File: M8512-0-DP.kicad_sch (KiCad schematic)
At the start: 1 part, among them J1 KL10_6-bay_backplane_connector

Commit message: Use pin NUMBERS not letters for backplane connector
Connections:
- net AA1: now also J1.1 (AA1); no longer J1.AA1
- net AA2: now also J1.2 (AA2); no longer J1.AA2
- net AB1: now also J1.3 (AB1); no longer J1.AB1
- net AB2: now also J1.4 (AB2); no longer J1.AB2
- net AC1: now also J1.5 (AC1); no longer J1.AC1
- net AC2: now also J1.6 (AC2); no longer J1.AC2
- net AD1: now also J1.7 (AD1); no longer J1.AD1
- net AD2: now also J1.8 (AD2); no longer J1.AD2
- net AE1: now also J1.9 (AE1); no longer J1.AE1
- net AE2: now also J1.10 (AE2); no longer J1.AE2
- net AF1: now also J1.11 (AF1); no longer J1.AF1
- net AF2: now also J1.12 (AF2); no longer J1.AF2
- net AH1: now also J1.13 (AH1); no longer J1.AH1
- net AH2: now also J1.14 (AH2); no longer J1.AH2
- net AJ1: now also J1.15 (AJ1); no longer J1.AJ1
- net AJ2: now also J1.16 (AJ2); no longer J1.AJ2
- net AK1: now also J1.17 (AK1); no longer J1.AK1
- net AK2: now also J1.18 (AK2); no longer J1.AK2
- net AL1: now also J1.19 (AL1); no longer J1.AL1
- net AL2: now also J1.20 (AL2); no longer J1.AL2
- net AM1: now also J1.21 (AM1); no longer J1.AM1
- net AM2: now also J1.22 (AM2); no longer J1.AM2
- net AN1: now also J1.23 (AN1); no longer J1.AN1
- net AN2: now also J1.24 (AN2); no longer J1.AN2
- net AP1: now also J1.25 (AP1); no longer J1.AP1
- net AP2: now also J1.26 (AP2); no longer J1.AP2
- net AR1: now also J1.27 (AR1); no longer J1.AR1
- net AR2: now also J1.28 (AR2); no longer J1.AR2
- net AS1: now also J1.29 (AS1); no longer J1.AS1
- net AS2: now also J1.30 (AS2); no longer J1.AS2
- net AT1: now also J1.31 (AT1); no longer J1.AT1
- net AT2: now also J1.32 (AT2); no longer J1.AT2
- net AU1: now also J1.33 (AU1); no longer J1.AU1
- net AU2: now also J1.34 (AU2); no longer J1.AU2
- net AV1: now also J1.35 (AV1); no longer J1.AV1
- net AV2: now also J1.36 (AV2); no longer J1.AV2
- net BA1: now also J1.37 (BA1); no longer J1.BA1
- net BA2: now also J1.38 (BA2); no longer J1.BA2
- net BB1: now also J1.39 (BB1); no longer J1.BB1
- net BB2: now also J1.40 (BB2); no longer J1.BB2
- net BC1: now also J1.41 (BC1); no longer J1.BC1
- net BC2: now also J1.42 (BC2); no longer J1.BC2
- net BD1: now also J1.43 (BD1); no longer J1.BD1
- net BD2: now also J1.44 (BD2); no longer J1.BD2
- net BE1: now also J1.45 (BE1); no longer J1.BE1
- net BE2: now also J1.46 (BE2); no longer J1.BE2
- net BF1: now also J1.47 (BF1); no longer J1.BF1
- net BF2: now also J1.48 (BF2); no longer J1.BF2
- net BH1: now also J1.49 (BH1); no longer J1.BH1
- net BH2: now also J1.50 (BH2); no longer J1.BH2
- net BJ1: now also J1.51 (BJ1); no longer J1.BJ1
- net BJ2: now also J1.52 (BJ2); no longer J1.BJ2
- net BK1: now also J1.53 (BK1); no longer J1.BK1
- net BK2: now also J1.54 (BK2); no longer J1.BK2
- net BL1: now also J1.55 (BL1); no longer J1.BL1
- net BL2: now also J1.56 (BL2); no longer J1.BL2
- net BM1: now also J1.57 (BM1); no longer J1.BM1
- net BM2: now also J1.58 (BM2); no longer J1.BM2
- net BN1: now also J1.59 (BN1); no longer J1.BN1
- net BN2: now also J1.60 (BN2); no longer J1.BN2
- net BP1: now also J1.61 (BP1); no longer J1.BP1
- net BP2: now also J1.62 (BP2); no longer J1.BP2
- net BR1: now also J1.63 (BR1); no longer J1.BR1
- net BR2: now also J1.64 (BR2); no longer J1.BR2
- net BS1: now also J1.65 (BS1); no longer J1.BS1
- net BS2: now also J1.66 (BS2); no longer J1.BS2
- net BT1: now also J1.67 (BT1); no longer J1.BT1
- net BT2: now also J1.68 (BT2); no longer J1.BT2
- net BU1: now also J1.69 (BU1); no longer J1.BU1
- net BU2: now also J1.70 (BU2); no longer J1.BU2
- net BV1: now also J1.71 (BV1); no longer J1.BV1
- net BV2: now also J1.72 (BV2); no longer J1.BV2
- net CA1: now also J1.73 (CA1); no longer J1.CA1
- net CB1: now also J1.75 (CB1); no longer J1.CB1
- net CB2: now also J1.76 (CB2); no longer J1.CB2
- net CC1: now also J1.77 (CC1); no longer J1.CC1
- net CC2: now also J1.78 (CC2); no longer J1.CC2
- net CD1: now also J1.79 (CD1); no longer J1.CD1
- net CD2: now also J1.80 (CD2); no longer J1.CD2
- net CE1: now also J1.81 (CE1); no longer J1.CE1
- net CE2: now also J1.82 (CE2); no longer J1.CE2
- net CF1: now also J1.83 (CF1); no longer J1.CF1
- net CF2: now also J1.84 (CF2); no longer J1.CF2
- net CH1: now also J1.85 (CH1); no longer J1.CH1
- net CH2: now also J1.86 (CH2); no longer J1.CH2
- net CJ1: now also J1.87 (CJ1); no longer J1.CJ1
- net CJ2: now also J1.88 (CJ2); no longer J1.CJ2
- net CK1: now also J1.89 (CK1); no longer J1.CK1
- net CK2: now also J1.90 (CK2); no longer J1.CK2
- net CL1: now also J1.91 (CL1); no longer J1.CL1
- net CL2: now also J1.92 (CL2); no longer J1.CL2
- net CM1: now also J1.93 (CM1); no longer J1.CM1
- net CM2: now also J1.94 (CM2); no longer J1.CM2
- net CN1: now also J1.95 (CN1); no longer J1.CN1
- net CN2: now also J1.96 (CN2); no longer J1.CN2
- net CP1: now also J1.97 (CP1); no longer J1.CP1
- net CP2: now also J1.98 (CP2); no longer J1.CP2
- net CR1: now also J1.99 (CR1); no longer J1.CR1
- net CR2: now also J1.100 (CR2); no longer J1.CR2
- net CS1: now also J1.101 (CS1); no longer J1.CS1
- net CS2: now also J1.102 (CS2); no longer J1.CS2
- net CT1: now also J1.103 (CT1); no longer J1.CT1
- net CT2: now also J1.104 (CT2); no longer J1.CT2
- net CU1: now also J1.105 (CU1); no longer J1.CU1
- net CU2: now also J1.106 (CU2); no longer J1.CU2
- net CV1: now also J1.107 (CV1); no longer J1.CV1
- net CV2: now also J1.108 (CV2), J1.74 (CA2); no longer J1.CA2, J1.CV2
- net DA1: now also J1.109 (DA1); no longer J1.DA1
- net DA2: now also J1.110 (DA2); no longer J1.DA2
- net DB1: now also J1.111 (DB1); no longer J1.DB1
- net DB2: now also J1.112 (DB2); no longer J1.DB2
- net DC1: now also J1.113 (DC1); no longer J1.DC1
- net DC2: now also J1.114 (DC2); no longer J1.DC2
- net DD1: now also J1.115 (DD1); no longer J1.DD1
- net DD2: now also J1.116 (DD2); no longer J1.DD2
- net DE1: now also J1.117 (DE1); no longer J1.DE1
- net DE2: now also J1.118 (DE2); no longer J1.DE2
- net DF1: now also J1.119 (DF1); no longer J1.DF1
- net DF2: now also J1.120 (DF2); no longer J1.DF2
- net DH1: now also J1.121 (DH1); no longer J1.DH1
- net DH2: now also J1.122 (DH2); no longer J1.DH2
- net DJ1: now also J1.123 (DJ1); no longer J1.DJ1
- net DJ2: now also J1.124 (DJ2); no longer J1.DJ2
- net DK1: now also J1.125 (DK1); no longer J1.DK1
- net DK2: now also J1.126 (DK2); no longer J1.DK2
- net DL1: now also J1.127 (DL1); no longer J1.DL1
- net DL2: now also J1.128 (DL2); no longer J1.DL2
- net DM1: now also J1.129 (DM1); no longer J1.DM1
- net DM2: now also J1.130 (DM2); no longer J1.DM2
- net DN1: now also J1.131 (DN1); no longer J1.DN1
- net DN2: now also J1.132 (DN2); no longer J1.DN2
- net DP1: now also J1.133 (DP1); no longer J1.DP1
- net DP2: now also J1.134 (DP2); no longer J1.DP2
- net DR1: now also J1.135 (DR1); no longer J1.DR1
- net DR2: now also J1.136 (DR2); no longer J1.DR2
- net DS1: now also J1.137 (DS1); no longer J1.DS1
- net DS2: now also J1.138 (DS2); no longer J1.DS2
- net DT1: now also J1.139 (DT1); no longer J1.DT1
- net DT2: now also J1.140 (DT2); no longer J1.DT2
- net DU1: now also J1.141 (DU1); no longer J1.DU1
- net DU2: now also J1.142 (DU2); no longer J1.DU2
- net DV1: now also J1.143 (DV1); no longer J1.DV1
- net DV2: now also J1.144 (DV2); no longer J1.DV2
- net EA1: now also J1.145 (EA1); no longer J1.EA1
- net EA2: now also J1.146 (EA2); no longer J1.EA2
- net EB1: now also J1.147 (EB1); no longer J1.EB1
- net EB2: now also J1.148 (EB2); no longer J1.EB2
- net EC1: now also J1.149 (EC1); no longer J1.EC1
- net EC2: now also J1.150 (EC2); no longer J1.EC2
- net ED1: now also J1.151 (ED1); no longer J1.ED1
- net ED2: now also J1.152 (ED2); no longer J1.ED2
- net EE1: now also J1.153 (EE1); no longer J1.EE1
- net EE2: now also J1.154 (EE2); no longer J1.EE2
- net EF1: now also J1.155 (EF1); no longer J1.EF1
- net EF2: now also J1.156 (EF2); no longer J1.EF2
- net EH1: now also J1.157 (EH1); no longer J1.EH1
- net EH2: now also J1.158 (EH2); no longer J1.EH2
- net EJ1: now also J1.159 (EJ1); no longer J1.EJ1
- net EJ2: now also J1.160 (EJ2); no longer J1.EJ2
- net EK1: now also J1.161 (EK1); no longer J1.EK1
- net EK2: now also J1.162 (EK2); no longer J1.EK2
- net EL1: now also J1.163 (EL1); no longer J1.EL1
- net EL2: now also J1.164 (EL2); no longer J1.EL2
- net EM1: now also J1.165 (EM1); no longer J1.EM1
- net EM2: now also J1.166 (EM2); no longer J1.EM2
- net EN1: now also J1.167 (EN1); no longer J1.EN1
- net EN2: now also J1.168 (EN2); no longer J1.EN2
- net EP1: now also J1.169 (EP1); no longer J1.EP1
- net EP2: now also J1.170 (EP2); no longer J1.EP2
- net ER1: now also J1.171 (ER1); no longer J1.ER1
- net ER2: now also J1.172 (ER2); no longer J1.ER2
- net ES1: now also J1.173 (ES1); no longer J1.ES1
- net ES2: now also J1.174 (ES2); no longer J1.ES2
- net ET1: now also J1.175 (ET1); no longer J1.ET1
- net ET2: now also J1.176 (ET2); no longer J1.ET2
- net EU1: now also J1.177 (EU1); no longer J1.EU1
- net EU2: now also J1.178 (EU2); no longer J1.EU2
- net EV1: now also J1.179 (EV1); no longer J1.EV1
- net EV2: now also J1.180 (EV2); no longer J1.EV2
- net FA1: now also J1.181 (FA1); no longer J1.FA1
- net FA2: now also J1.182 (FA2); no longer J1.FA2
- net FB1: now also J1.183 (FB1); no longer J1.FB1
- net FB2: now also J1.184 (FB2); no longer J1.FB2
- net FC1: now also J1.185 (FC1); no longer J1.FC1
- net FC2: now also J1.186 (FC2); no longer J1.FC2
- net FD1: now also J1.187 (FD1); no longer J1.FD1
- net FD2: now also J1.188 (FD2); no longer J1.FD2
- net FE1: now also J1.189 (FE1); no longer J1.FE1
- net FE2: now also J1.190 (FE2); no longer J1.FE2
- net FF1: now also J1.191 (FF1); no longer J1.FF1
- net FF2: now also J1.192 (FF2); no longer J1.FF2
- net FH1: now also J1.193 (FH1); no longer J1.FH1
- net FH2: now also J1.194 (FH2); no longer J1.FH2
- net FJ1: now also J1.195 (FJ1); no longer J1.FJ1
- net FJ2: now also J1.196 (FJ2); no longer J1.FJ2
- net FK1: now also J1.197 (FK1); no longer J1.FK1
- net FK2: now also J1.198 (FK2); no longer J1.FK2
- net FL1: now also J1.199 (FL1); no longer J1.FL1
- net FL2: now also J1.200 (FL2); no longer J1.FL2
- net FM1: now also J1.201 (FM1); no longer J1.FM1
- net FM2: now also J1.202 (FM2); no longer J1.FM2
- net FN1: now also J1.203 (FN1); no longer J1.FN1
- net FN2: now also J1.204 (FN2); no longer J1.FN2
- net FP1: now also J1.205 (FP1); no longer J1.FP1
- net FP2: now also J1.206 (FP2); no longer J1.FP2
- net FR1: now also J1.207 (FR1); no longer J1.FR1
- net FR2: now also J1.208 (FR2); no longer J1.FR2
- net FS1: now also J1.209 (FS1); no longer J1.FS1
- net FS2: now also J1.210 (FS2); no longer J1.FS2
- net FT1: now also J1.211 (FT1); no longer J1.FT1
- net FT2: now also J1.212 (FT2); no longer J1.FT2
- net FU1: now also J1.213 (FU1); no longer J1.FU1
- net FU2: now also J1.214 (FU2); no longer J1.FU2
- net FV1: now also J1.215 (FV1); no longer J1.FV1
- net FV2: now also J1.216 (FV2); no longer J1.FV2

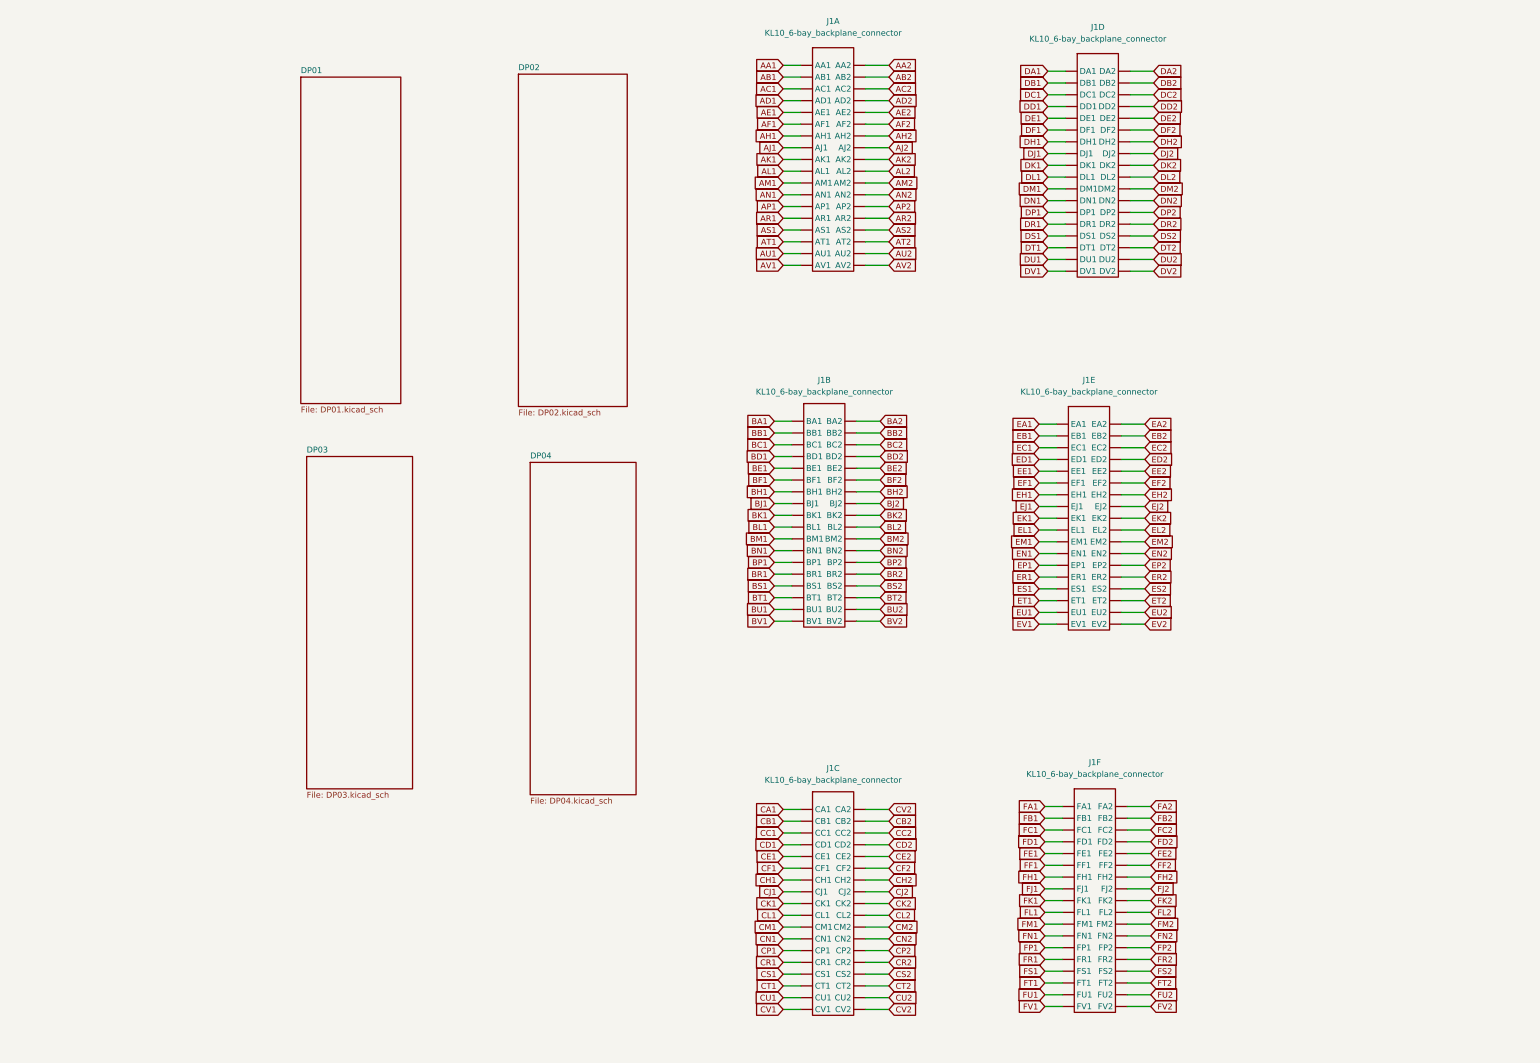
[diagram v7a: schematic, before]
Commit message: Nearly done switching to <ABn> backplane labels
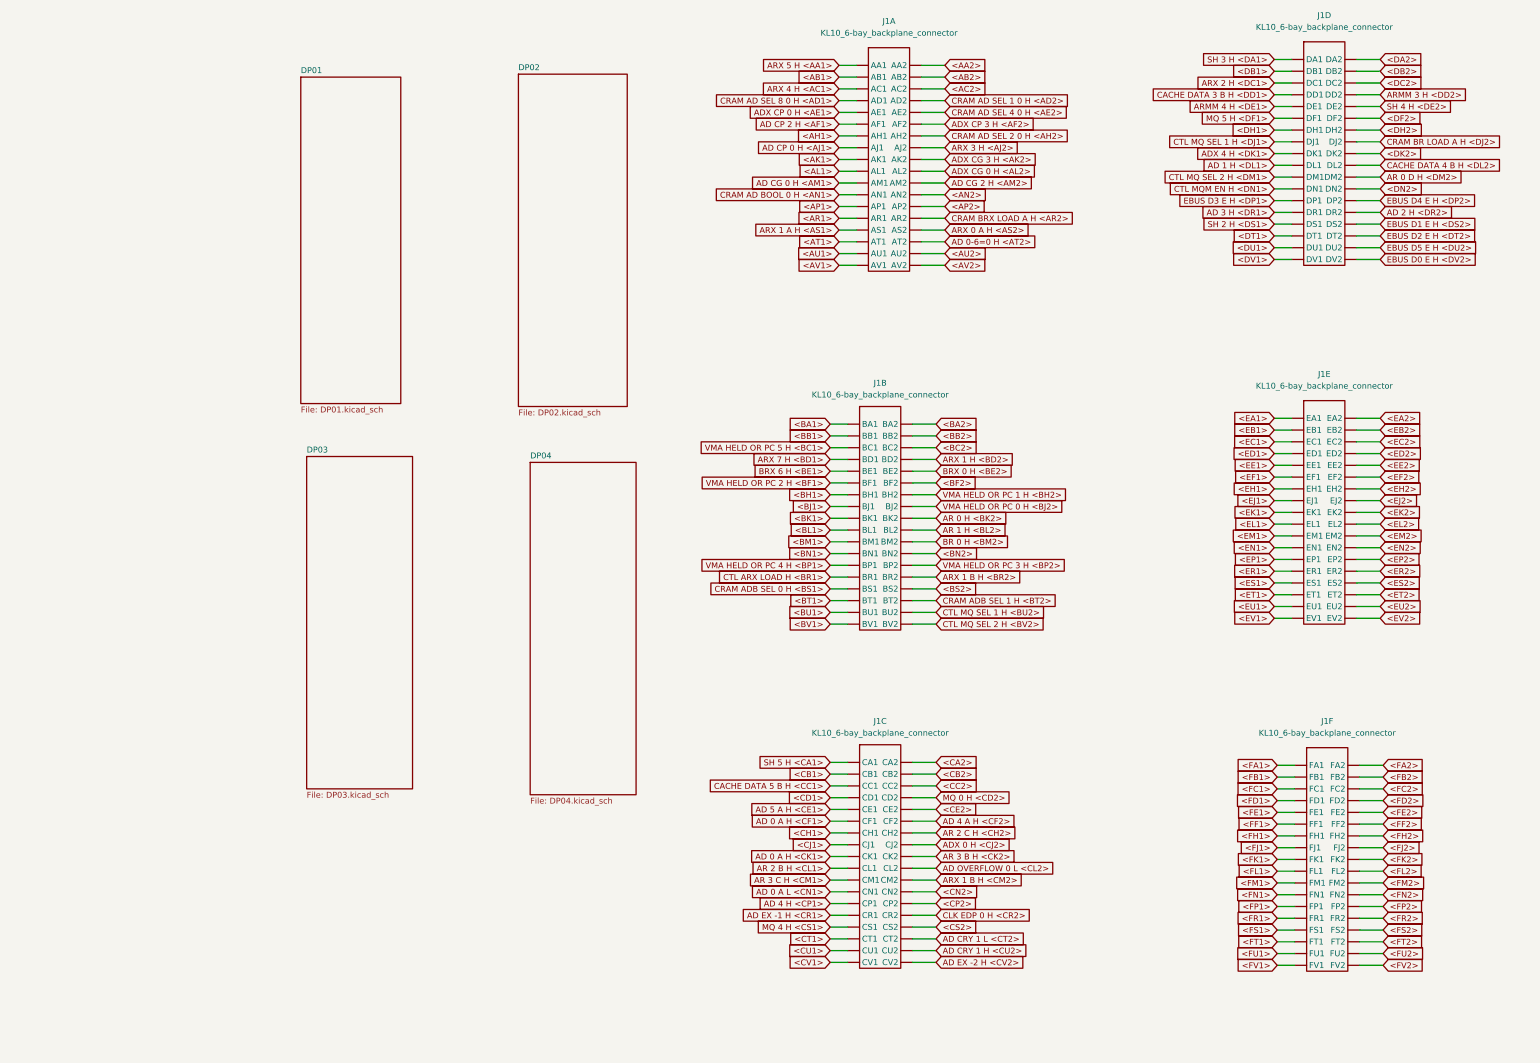
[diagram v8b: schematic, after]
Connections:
- net AA1 renamed ARX 5 H <AA1>
- net AA2 renamed <AA2>
- net AB1 renamed <AB1>
- net AB2 renamed <AB2>
- net AC1 renamed ARX 4 H <AC1>
- net AC2 renamed <AC2>
- net AD1 renamed CRAM AD SEL 8 0 H <AD1>
- net AD2 renamed CRAM AD SEL 1 0 H <AD2>
- net AE1 renamed ADX CP 0 H <AE1>
- net AE2 renamed CRAM AD SEL 4 0 H <AE2>
- net AF1 renamed AD CP 2 H <AF1>
- net AF2 renamed ADX CP 3 H <AF2>
- net AH1 renamed <AH1>
- net AH2 renamed CRAM AD SEL 2 0 H <AH2>
- net AJ1 renamed AD CP 0 H <AJ1>
- net AJ2 renamed ARX 3 H <AJ2>
- net AK1 renamed <AK1>
- net AK2 renamed ADX CG 3 H <AK2>
- net AL1 renamed <AL1>
- net AL2 renamed ADX CG 0 H <AL2>
- net AM1 renamed AD CG 0 H <AM1>
- net AM2 renamed AD CG 2 H <AM2>
- net AN1 renamed CRAM AD BOOL 0 H <AN1>
- net AN2 renamed <AN2>
- net AP1 renamed <AP1>
- net AP2 renamed <AP2>
- net AR1 renamed <AR1>
- net AR2 renamed CRAM BRX LOAD A H <AR2>
- net AS1 renamed ARX 1 A H <AS1>
- net AS2 renamed ARX 0 A H <AS2>
- net AT1 renamed <AT1>
- net AT2 renamed AD 0-6=0 H <AT2>
- net AU1 renamed <AU1>
- net AU2 renamed <AU2>
- net AV1 renamed <AV1>
- net AV2 renamed <AV2>
- net BA1 renamed <BA1>
- net BA2 renamed <BA2>
- net BB1 renamed <BB1>
- net BB2 renamed <BB2>
- net BC1 renamed VMA HELD OR PC 5 H <BC1>
- net BC2 renamed <BC2>
- net BD1 renamed ARX 7 H <BD1>
- net BD2 renamed ARX 1 H <BD2>
- net BE1 renamed BRX 6 H <BE1>
- net BE2 renamed BRX 0 H <BE2>
- net BF1 renamed VMA HELD OR PC 2 H <BF1>
- net BF2 renamed <BF2>
- net BH1 renamed <BH1>
- net BH2 renamed VMA HELD OR PC 1 H <BH2>
- net BJ1 renamed <BJ1>
- net BJ2 renamed VMA HELD OR PC 0 H <BJ2>
- net BK1 renamed <BK1>
- net BK2 renamed AR 0 H <BK2>
- net BL1 renamed <BL1>
- net BL2 renamed AR 1 H <BL2>
- net BM1 renamed <BM1>
- net BM2 renamed BR 0 H <BM2>
- net BN1 renamed <BN1>
- net BN2 renamed <BN2>
- net BP1 renamed VMA HELD OR PC 4 H <BP1>
- net BP2 renamed VMA HELD OR PC 3 H <BP2>
- net BR1 renamed CTL ARX LOAD H <BR1>
- net BR2 renamed ARX 1 B H <BR2>
- net BS1 renamed CRAM ADB SEL 0 H <BS1>
- net BS2 renamed <BS2>
- net BT1 renamed <BT1>
- net BT2 renamed CRAM ADB SEL 1 H <BT2>
- net BU1 renamed <BU1>
- net BU2 renamed CTL MQ SEL 1 H <BU2>
- net BV1 renamed <BV1>
- net BV2 renamed CTL MQ SEL 2 H <BV2>
- net CA1 renamed SH 5 H <CA1>
- net CB1 renamed <CB1>
- net CB2 renamed <CB2>
- net CC1 renamed CACHE DATA 5 B H <CC1>
- net CC2 renamed <CC2>
- net CD1 renamed <CD1>
- net CD2 renamed MQ 0 H <CD2>
- net CE1 renamed AD 5 A H <CE1>
- net CE2 renamed <CE2>
- net CF1 renamed AD 0 A H <CF1>
- net CF2 renamed AD 4 A H <CF2>
- net CH1 renamed <CH1>
- net CH2 renamed AR 2 C H <CH2>
- net CJ1 renamed <CJ1>
- net CJ2 renamed ADX 0 H <CJ2>
- net CK1 renamed AD 0 A H <CK1>
- net CK2 renamed AR 3 B H <CK2>
- net CL1 renamed AR 2 B H <CL1>
- net CL2 renamed AD OVERFLOW 0 L <CL2>
- net CM1 renamed AR 3 C H <CM1>
- net CM2 renamed ARX 1 B H <CM2>
- net CN1 renamed AD 0 A L <CN1>
- net CN2 renamed <CN2>
- net CP1 renamed AD 4 H <CP1>
- net CP2 renamed <CP2>
- net CR1 renamed AD EX -1 H <CR1>
- net CR2 renamed CLK EDP 0 H <CR2>
- net CS1 renamed MQ 4 H <CS1>
- net CS2 renamed <CS2>
- net CT1 renamed <CT1>
- net CT2 renamed AD CRY 1 L <CT2>
- net CU1 renamed <CU1>
- net CU2 renamed AD CRY 1 H <CU2>
- net CV1 renamed <CV1>
- net CV2 renamed <CA2>
- net <CA2>: no longer J1.108 (CV2)
- net DA1 renamed SH 3 H <DA1>
- net DA2 renamed <DA2>
- net DB1 renamed <DB1>
- net DB2 renamed <DB2>
- net DC1 renamed ARX 2 H <DC1>
- net DC2 renamed <DC2>
- net DD1 renamed CACHE DATA 3 B H <DD1>
- net DD2 renamed ARMM 3 H <DD2>
- net DE1 renamed ARMM 4 H <DE1>
- net DE2 renamed SH 4 H <DE2>
- net DF1 renamed MQ 5 H <DF1>
- net DF2 renamed <DF2>
- net DH1 renamed <DH1>
- net DH2 renamed <DH2>
- net DJ1 renamed CTL MQ SEL 1 H <DJ1>
- net DJ2 renamed CRAM BR LOAD A H <DJ2>
- net DK1 renamed ADX 4 H <DK1>
- net DK2 renamed <DK2>
- net DL1 renamed AD 1 H <DL1>
- net DL2 renamed CACHE DATA 4 B H <DL2>
- net DM1 renamed CTL MQ SEL 2 H <DM1>
- net DM2 renamed AR 0 D H <DM2>
- net DN1 renamed CTL MQM EN H <DN1>
- net DN2 renamed <DN2>
- net DP1 renamed EBUS D3 E H <DP1>
- net DP2 renamed EBUS D4 E H <DP2>
- net DR1 renamed AD 3 H <DR1>
- net DR2 renamed AD 2 H <DR2>
- net DS1 renamed SH 2 H <DS1>
- net DS2 renamed EBUS D1 E H <DS2>
- net DT1 renamed <DT1>
- net DT2 renamed EBUS D2 E H <DT2>
- net DU1 renamed <DU1>
- net DU2 renamed EBUS D5 E H <DU2>
- net DV1 renamed <DV1>
- net DV2 renamed EBUS D0 E H <DV2>
- net EA1 renamed <EA1>
- net EA2 renamed <EA2>
- net EB1 renamed <EB1>
- net EB2 renamed <EB2>
- net EC1 renamed <EC1>
- net EC2 renamed <EC2>
- net ED1 renamed <ED1>
- net ED2 renamed <ED2>
- net EE1 renamed <EE1>
- net EE2 renamed <EE2>
- net EF1 renamed <EF1>
- net EF2 renamed <EF2>
- net EH1 renamed <EH1>
- net EH2 renamed <EH2>
- net EJ1 renamed <EJ1>
- net EJ2 renamed <EJ2>
- net EK1 renamed <EK1>
- net EK2 renamed <EK2>
- net EL1 renamed <EL1>
- net EL2 renamed <EL2>
- net EM1 renamed <EM1>
- net EM2 renamed <EM2>
- net EN1 renamed <EN1>
- net EN2 renamed <EN2>
- net EP1 renamed <EP1>
- net EP2 renamed <EP2>
- net ER1 renamed <ER1>
- net ER2 renamed <ER2>
- net ES1 renamed <ES1>
- net ES2 renamed <ES2>
- net ET1 renamed <ET1>
- net ET2 renamed <ET2>
- net EU1 renamed <EU1>
- net EU2 renamed <EU2>
- net EV1 renamed <EV1>
- net EV2 renamed <EV2>
- net FA1 renamed <FA1>
- net FA2 renamed <FA2>
- net FB1 renamed <FB1>
- net FB2 renamed <FB2>
- net FC1 renamed <FC1>
- net FC2 renamed <FC2>
- net FD1 renamed <FD1>
- net FD2 renamed <FD2>
- net FE1 renamed <FE1>
- net FE2 renamed <FE2>
- net FF1 renamed <FF1>
- net FF2 renamed <FF2>
- net FH1 renamed <FH1>
- net FH2 renamed <FH2>
- net FJ1 renamed <FJ1>
- net FJ2 renamed <FJ2>
- net FK1 renamed <FK1>
- net FK2 renamed <FK2>
- net FL1 renamed <FL1>
- net FL2 renamed <FL2>
- net FM1 renamed <FM1>
- net FM2 renamed <FM2>
- net FN1 renamed <FN1>
- net FN2 renamed <FN2>
- net FP1 renamed <FP1>
- net FP2 renamed <FP2>
- net FR1 renamed <FR1>
- net FR2 renamed <FR2>
- net FS1 renamed <FS1>
- net FS2 renamed <FS2>
- net FT1 renamed <FT1>
- net FT2 renamed <FT2>
- net FU1 renamed <FU1>
- net FU2 renamed <FU2>
- net FV1 renamed <FV1>
- net FV2 renamed <FV2>
- new net AD EX -2 H <CV2>: J1.108 (CV2)
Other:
- moved on the sheet: J1A, J1B, J1C, J1D, J1E, J1F
